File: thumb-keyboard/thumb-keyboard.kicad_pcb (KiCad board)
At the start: 2 copper layers, 144 x 60 mm, 198 parts, among them J1 Conn_01x02_Socket, U1 nice_nano

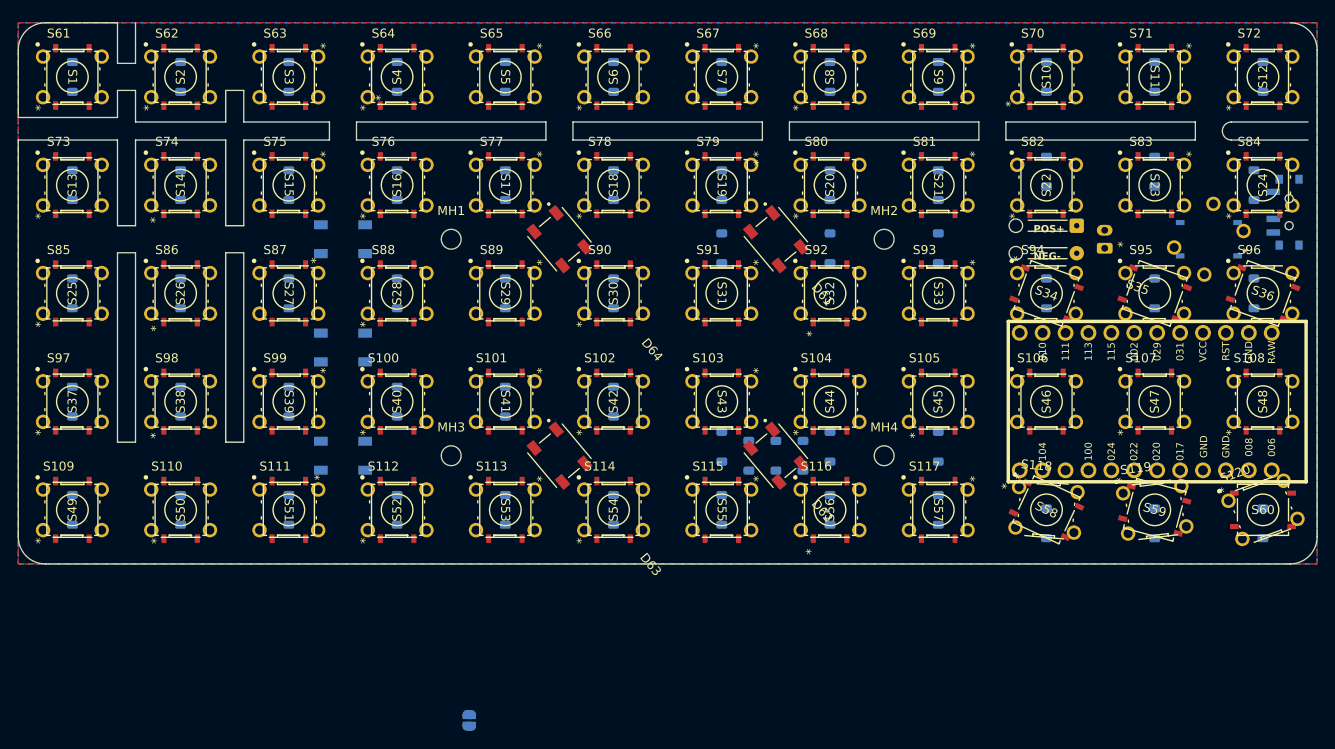
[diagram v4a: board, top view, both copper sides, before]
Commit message: have something that looks alright. max size of 144x60mm. A little concerning how messy it is though
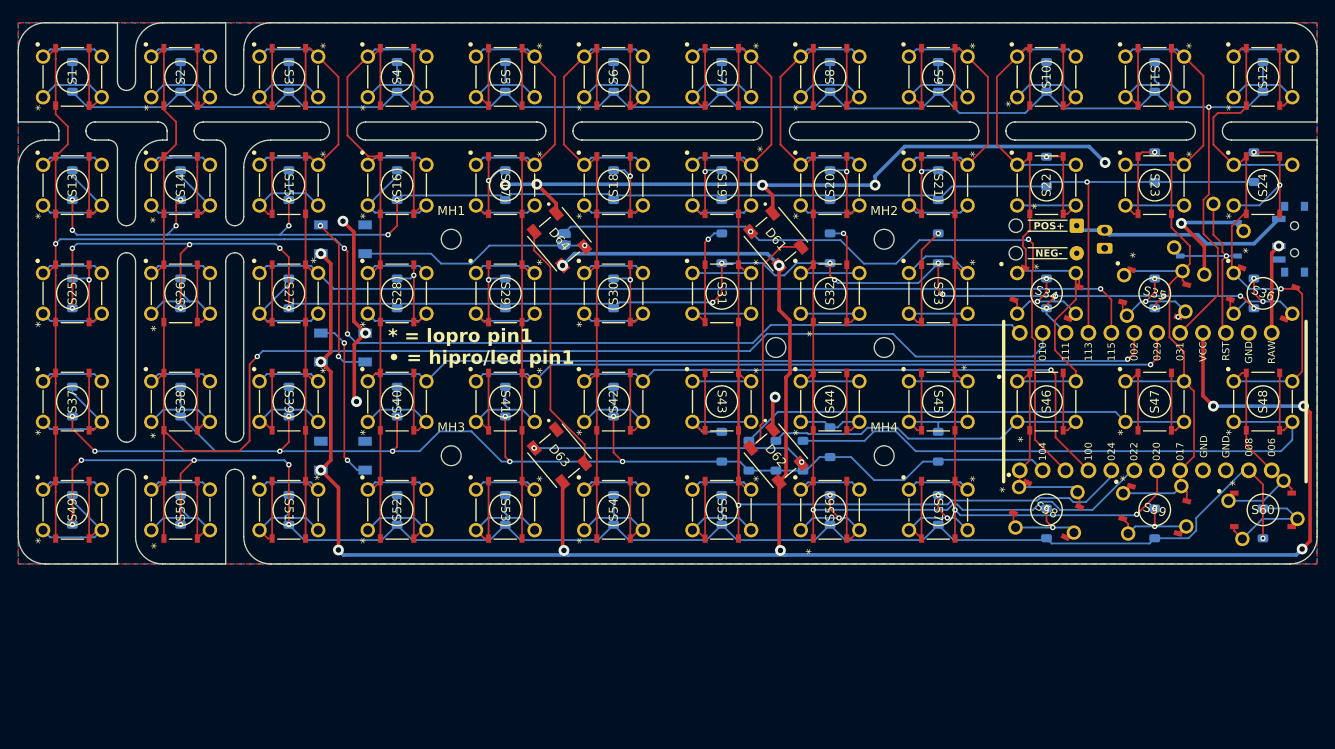
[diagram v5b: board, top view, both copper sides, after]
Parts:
- added BATT STANDOFF: MountingHole_2.2mm_M2, MountingHole:MountingHole_2.2mm_M2, F.Cu at (141.0, 84.0)
- added REF**: MountingHole_2.2mm_M2, MountingHole:MountingHole_2.2mm_M2, F.Cu at (153.0, 84.0)
- moved JumpIfNoFrontLED 54.4 mm to (117.5, 72.0), turned to 90 degrees
- moved S121 3.06 mm to (198.5, 72.0)
- moved D24 2.00 mm to (194.0, 64.0)
- moved D23 0.50 mm to (183.0, 64.0)
- moved D44 0.50 mm to (147.0, 94.5)
- turned S34 to -19 degrees
- turned S35 to -15 degrees
- turned S45 to -90 degrees
- turned S95 to 4 degrees
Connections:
- S121 pad SH1: (no net) -> /GND
- S121 pad SH2: (no net) -> /GND
- S121 pad SH3: (no net) -> /GND
- S121 pad SH4: (no net) -> /GND
- U1 pad 11: /COL0 -> /ROW3
- U1 pad 13: /COL6 -> /COL0
- U1 pad 14: /COL5 -> /COL1
- U1 pad 15: /COL4 -> /ROW2
- U1 pad 16: /COL2 -> /ROW1
- U1 pad 17: /ROW1 -> /COL2
- U1 pad 18: /ROW0 -> /COL3
- U1 pad 19: /ROW3 -> /COL4
- U1 pad 20: /COL10 -> /ROW0
- U1 pad 6: /COL7 -> /COL8
- U1 pad 7: /COL9 -> /COL7
- U1 pad 8: /COL8 -> /COL6
- U1 pad 9: /COL3 -> /COL5
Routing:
- net /VCC: track 0.00 -> 244.7 mm, vias 0 -> 11
- net /COL0: track 0.00 -> 219.5 mm, vias 0 -> 3
- net /COL1: track 0.00 -> 213.8 mm, vias 0 -> 1
- net /COL2: track 0.00 -> 200.4 mm, vias 0 -> 1
- net /COL3: track 0.00 -> 190.6 mm, vias 0 -> 1
- net /COL4: track 0.00 -> 180.2 mm, vias 0 -> 1
- net /ROW0: track 0.00 -> 176.2 mm, vias 0 -> 1
- net /ROW4: track 0.00 -> 173.5 mm, vias 0 -> 7
- net /ROW2: track 0.00 -> 171.8 mm, vias 0 -> 18
- net /ROW1: track 0.00 -> 166.4 mm, vias 0 -> 9
- net /COL5: track 0.00 -> 165.9 mm, vias 0 -> 1
- net /COL6: track 0.00 -> 161.7 mm, vias 0 -> 1
- net /COL7: track 0.00 -> 151.0 mm, vias 0 -> 1
- net /ROW3: track 0.00 -> 140.2 mm, vias 0 -> 10
- net /COL8: track 0.00 -> 134.0 mm, vias 0 -> 2
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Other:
- outline, holes or cut-outs redrawn
- board text added: "* = lopro pin1 • = hipro/led pin1"
- board text added: "301230"
- board text added: "BATT STAND- OFF MOUNT HOLES"
- board text added: "jump if no front leds"
- board text removed: "*"
- board text removed: "301230 battery"

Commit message: sent out v1.0 pcb order
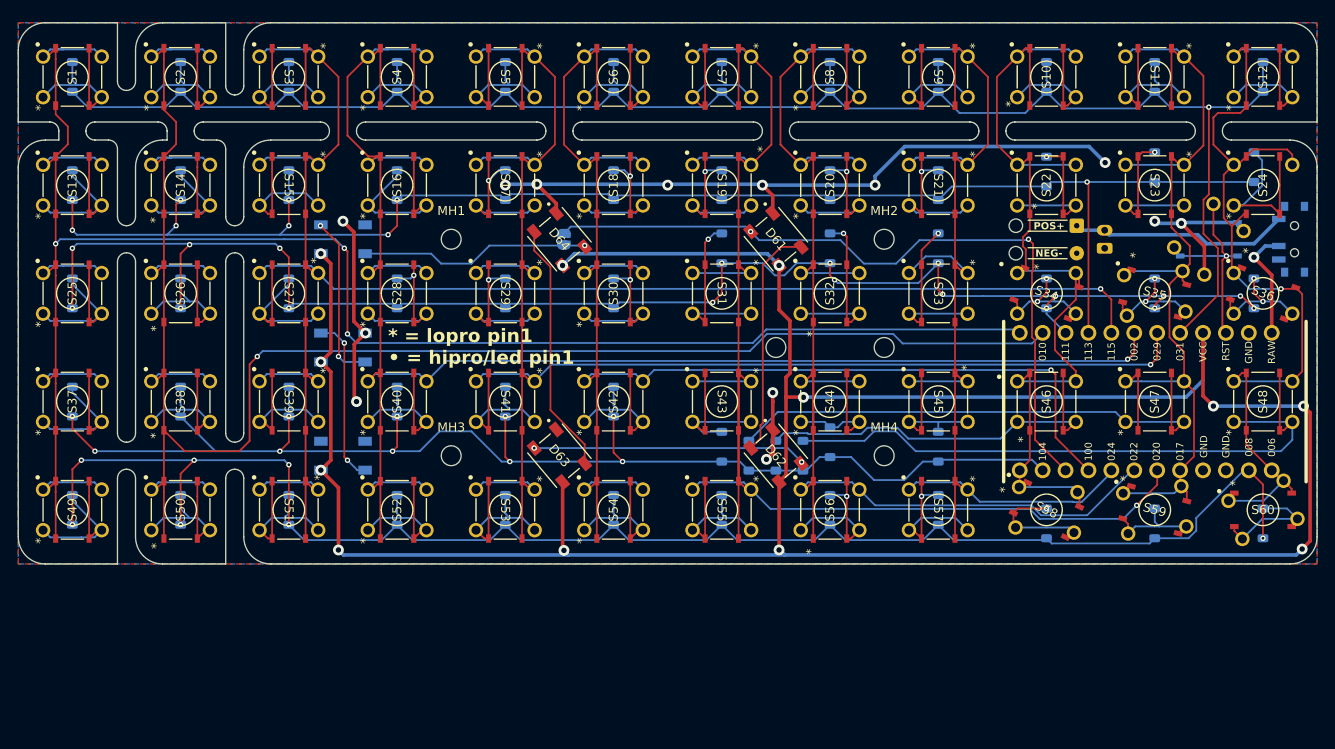
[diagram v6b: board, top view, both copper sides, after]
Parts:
- added G***: LOGO, thummingbird:thummingbird, B.Cu at (103.5, 85.5)
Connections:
- S121 pad SH1: /GND -> (no net)
- S121 pad SH2: /GND -> (no net)
- S121 pad SH3: /GND -> (no net)
- S121 pad SH4: /GND -> (no net)
- U1 pad 6: /COL8 -> /COL6
- U1 pad 8: /COL6 -> /COL8
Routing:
- net /VCC: track 244.7 -> 297.1 mm, vias 11 -> 12
- net /COL8: track 134.0 -> 125.8 mm, vias 2 -> 0
- net /GND: track 117.1 -> 124.1 mm, vias 10 -> 13
- net /COL6: track 161.7 -> 167.5 mm
- net /COL7: track 151.0 -> 146.1 mm, vias 1 -> 0
- net /C11R1D: track 15.7 -> 20.2 mm, vias 2 -> 0
- net /C0R2D: track 17.4 -> 20.7 mm, vias 1 -> 0
- net /CHARGE+: track 9.95 -> 12.5 mm
- net /COL1: track 213.8 -> 211.7 mm
- net /COL11: track 98.6 -> 100.2 mm
- net /C9R4D: track 12.0 -> 13.4 mm, vias 2 -> 1
- net /C7R4D: track 18.7 -> 17.7 mm, vias 2 -> 1
- net /C8R4D: track 18.7 -> 17.7 mm, vias 2 -> 1
- net /C10R2D: track 13.3 -> 13.5 mm, vias 3 -> 2
- net /C10R4D: track 11.9 -> 12.1 mm, vias 2 -> 0
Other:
- outline, holes or cut-outs redrawn
- board text added: "github.com/rileytuttle/thummingboard Thummingboard V1.0"
